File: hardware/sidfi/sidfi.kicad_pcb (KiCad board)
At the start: 2 copper layers, 150 x 65 mm, 45 parts, among them J1 ICSP, J2 SD_CARD, J3 USB_B, J4 AUDIO_OUT, J5 LCD_KEYS, Q1 2N3904, U1 74HCT164, U2 74HCT164, U3 MCP1700-3302E_TO92, U4 74HC148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

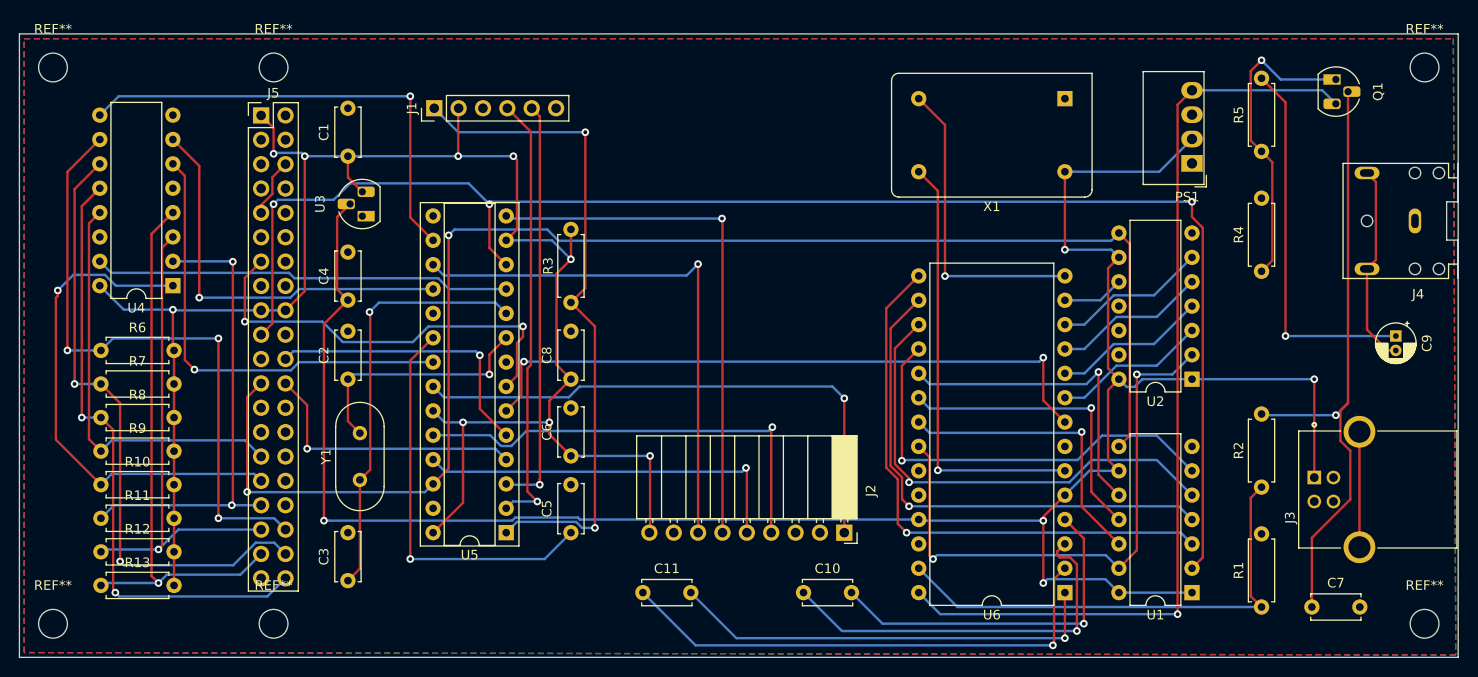
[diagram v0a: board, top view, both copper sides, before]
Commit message: Route the PCB
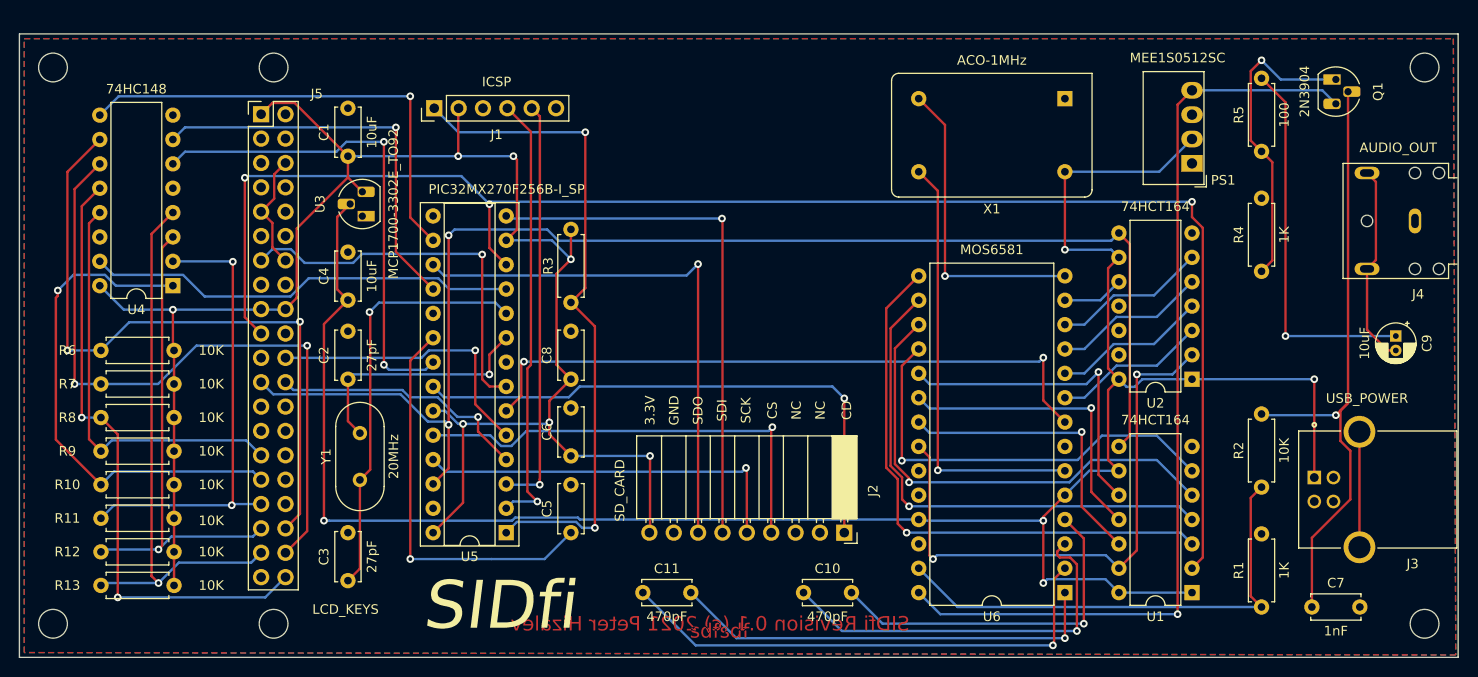
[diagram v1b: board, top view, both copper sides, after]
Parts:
- J3: value USB_B -> USB_POWER
- moved J5 0.12 mm to (99.7, 79.9)
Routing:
- net 6581_LCD_SCK: track 152.4 -> 142.1 mm
- net KEY_2: track 65.0 -> 72.5 mm
- net GND: track 38.3 -> 44.4 mm
- net 6581_LCD_SDO: track 158.0 -> 163.3 mm
- net KEY_1: track 65.9 -> 71.1 mm, vias 3 -> 2
- net KEY_CODE2: track 47.6 -> 51.9 mm, vias 1 -> 2
- net LCD_RESET: track 44.5 -> 40.4 mm, vias 2 -> 1
- net LCD_CS: track 29.0 -> 27.2 mm
- net KEY_CODE_EO: track 43.6 -> 45.1 mm
- net VCC: track 190.6 -> 189.4 mm, vias 9 -> 7
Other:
- board text added: "3.3V"
- board text added: "CD"
- board text added: "CS"
- board text added: "GND"
- board text added: "NC"
- board text added: "SCK"
- board text added: "SDI"
- board text added: "SDO"
- board text added: "SIDfi"
- board text added: "SIDfi Revision 0.1 (c) 2021 Peter Hizalev"
- board text added: "SIDfi Version 0.1 (c) 2021 Peter Hizalev"
- board text added: "sdfsdf"

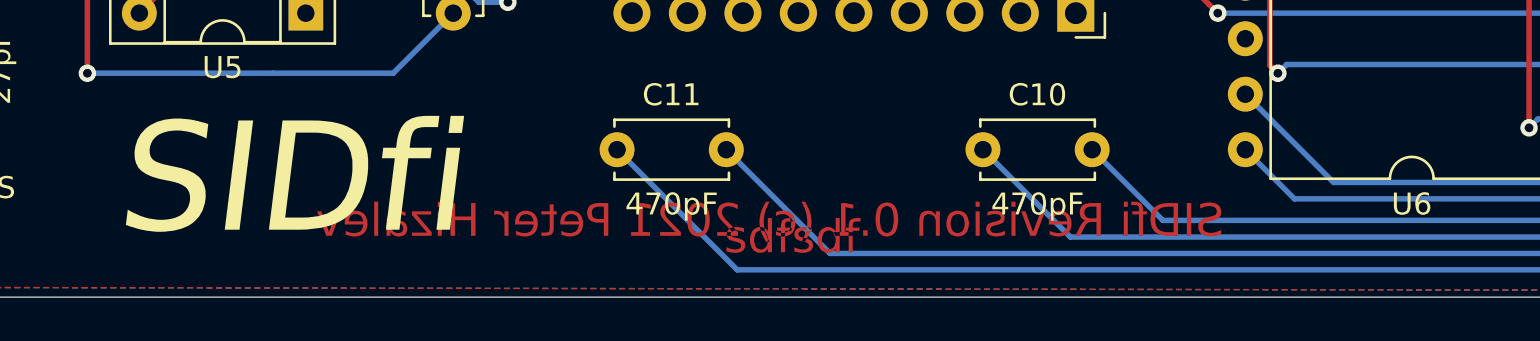
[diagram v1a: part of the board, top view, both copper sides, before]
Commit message: Remove accidental objects in PCB
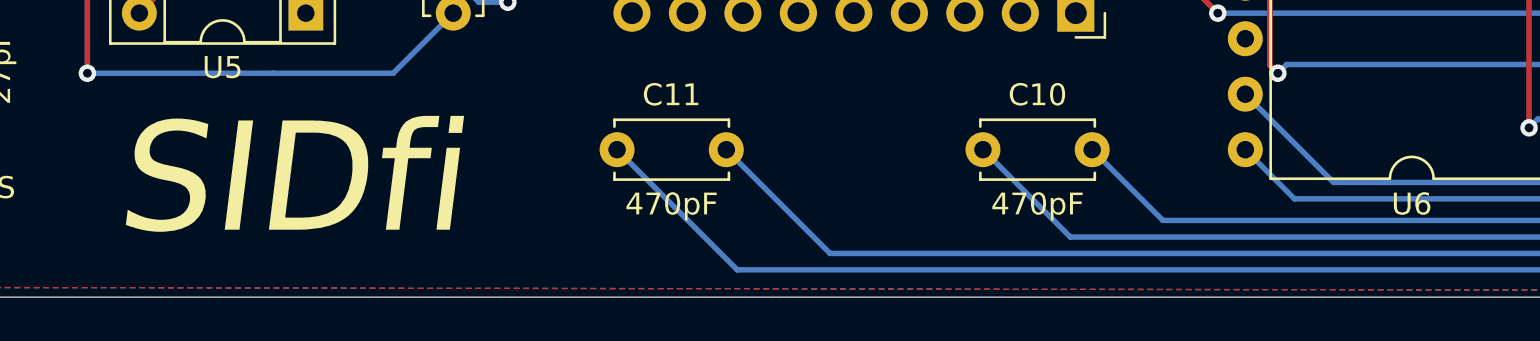
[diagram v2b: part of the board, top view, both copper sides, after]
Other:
- board text removed: "SIDfi Revision 0.1 (c) 2021 Peter Hizalev"
- board text removed: "sdfsdf"
